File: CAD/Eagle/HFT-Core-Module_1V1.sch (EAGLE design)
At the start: 399 parts, among them Q0521 ABS07-32.768KHZ, Q0811 ABM03B-32.000MHZ, Q0911 ABM3B-16MHZ-10-R50-1-U, T1201 MMBT2222, T1202 MMBT2222, T1203 MMBT2222, U0111 STM32L4Z_144PIN_SMPS, U0431 PAM2305AAB120, U0601 LM4120IM5-3.0, U0611 MAX5217, U0631 CFPT-141-20MHZ, U0641 OPA354, U0701 Si5338, U0801 SX1276, U0901 AX5243, U0911 PE4259, U0921 PE4259, U0991 PE4259, U1101 MCP3911A0-E-SS, U1111 MAX5136AGTG+, U1131 OPA354, U1141 OPA354, U1201 NHD-C0220BIZ_2X20CHARS, U1301 MPU-9250, U1311 MS5607-02BA03, U1321 SHT31-DIS, U1402 SPV1040T, U1501 TS5A23166, U1601 SC189ZSKTRT, U1701 TS5A23166, U1801 TS5A23166, U1901 TS5A23166, X1261 TTE_EN11-HSM, X1401 WIRE-TO-BOARD_5MM08_1X02, X2001 MOLEX 105017-0001, X2101 SMA_SMT_AMPHENOL-901-143, SAM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, X2111 SMA_SMT_AMPHENOL-901-143, SAM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, X2201 CUI SJ1-3535NS, X2211 CUI SJ1-3535NS, X2311 2X20/90_1MM27_HARWIN_M50-3202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, X2312 2X20/90_1MM27_HARWIN_M50-3202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, X2321 2X20/90_1MM27_HARWIN_M50-3202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, X2322 2X20/90_1MM27_HARWIN_M50-3202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, X2331 2X20/90_1MM27_HARWIN_M50-3202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, X2332 2X20/90_1MM27_HARWIN_M50-3202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

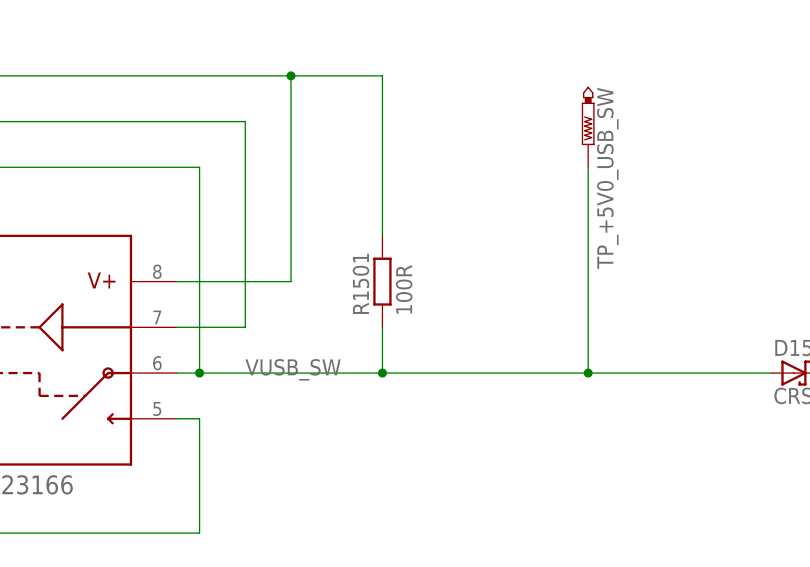
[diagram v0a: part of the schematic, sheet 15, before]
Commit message: HW_1V1 - USB-SW - Bybass resistor changed to 68R
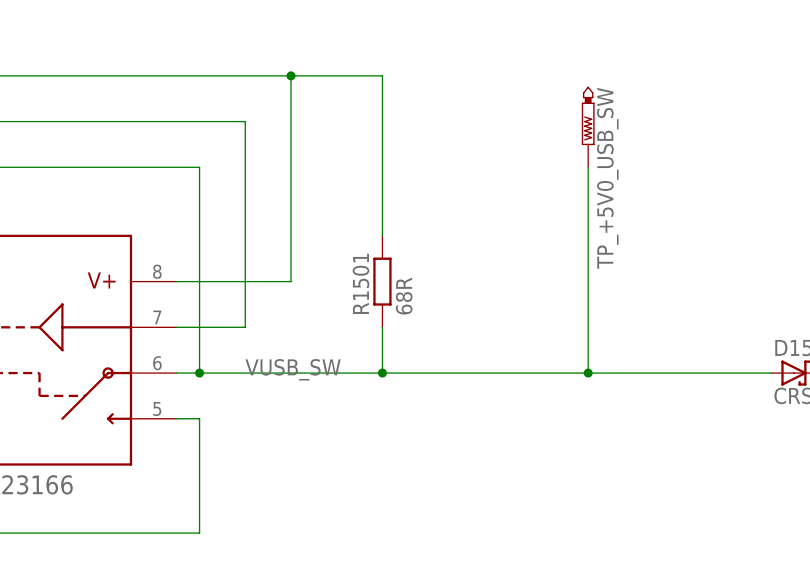
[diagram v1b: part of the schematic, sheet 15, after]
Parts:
- R1501: value 100R -> 68R
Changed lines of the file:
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@@
 <part name="R1412" library="rcl" deviceset="R-EU_" device="R0603" value="100kR"/>
 <part name="X1401" library="df4iah_connector" deviceset="WIRE-TO-BOARD_5MM08_1X02" device=""/>
-<part name="R1501" library="df4iah_rcl" deviceset="R-EU_" device="R0805" value="100R"/>
+<part name="R1501" library="df4iah_rcl" deviceset="R-EU_" device="R0805" value="68R"/>
 <part name="R0331" library="rcl" deviceset="R-EU_" device="R0603" value="100kR"/>
 <part name="R0332" library="rcl" deviceset="R-EU_" device="R0603" value="100kR"/>

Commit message: HW_1V1 - CAD/Eagle - Replacements for 9-axis controller and 1.8V supply
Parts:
- removed C0431, C0444: 10uF, rcl:C-EUC0805
- removed C0432: 100nF, rcl:C-EUC0603
- removed L0433: 2.2uH 14mR, df4iah_rcl:L-EU6.0X6.0MM
- removed TP_+1V2: PTR1B1,27, testpad:PTR1B1,27
- removed U0431: PAM2305AAB120, df4iah_powersupply:PAM2305
- added C0001, C0003: 10uF, rcl:C-EUC0805
- added C0002: 100nF, rcl:C-EUC0603
- added L0001: 2.2uH 14mR, df4iah_rcl:L-EU6.0X6.0MM
- added TP_+1V1: PTR1B1,27, testpad:PTR1B1,27
- added U0001: PAM2305AAB120, df4iah_powersupply:PAM2305
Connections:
- net +1V8_UNUSED renamed +1V8
- net +1V2: now also C0003.1, L0001.1, TP_+1V1.TP, U0001.VOUT_FB; no longer C0444.1, L0433.1, TP_+1V2.TP, U0431.VOUT_FB
- net +3V3: now also C0001.1, C0002.1, U0001.EN, U0001.VIN; no longer C0431.1, C0432.1, U0431.EN, U0431.VIN
- net GND: now also C0001.2, C0002.2, C0003.2, U0001.GND; no longer C0431.2, C0432.2, C0444.2, U0431.GND
- net VDD12_SW: now also L0001.2, U0001.SW; no longer L0433.2, U0431.SW
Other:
- note added: "12mA Start-up mode 2mA MPPT mode TODO: To be replaced by Texas Instruments BQ25570"
- note added: "MCU LF Osc"
- note added: "MCU Reset & SWD"
- note added: "MCU power distribution"
- note added: "MCU: low frequency oscillator"
- note added: "Power converter 3.3V --> 1.2V"
- note added: "Power converter 3.3V --> 1.8V"
- note added: "TODO: To be replaced by ICM-20948 (1.8 Volt !) Use SPI instead of I2C and Level Converter"
- note added: "VCTCXO 20MHz"
- note removed: "12mA Start-up mode 2mA MPPT mode"
- note removed: "Low frequency oscillator"

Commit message: HW_1V1 - CAD/Eagle - some more changes
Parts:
- removed C1301, C1303: 100nF, rcl:C-EUC0603
- removed C1302: 10nF, rcl:C-EUC0603
- removed D1403: CRS08, df4iah_diode:CRS08
- removed R1301: 68R, rcl:R-EU_R0603
- removed U1301: MPU-9250, df4iah_sensors:MPU-9250
- removed U1402: SPV1040T, df4iah_powersupply:SPV1040
- added C0004, C0005, C0007: 100nF, rcl:C-EUC0603
- added C0006: 10nF, rcl:C-EUC0603
- added R0001: 68R, rcl:R-EU_R0603
- added R0002, R0003: 68R, df4iah_rcl:R-EU_R0805
- added R0004, R0005: 2M, df4iah_rcl:R-EU_R0805
- added U0004: TS5A23166, df4iah_sc-switches:TS5A23166
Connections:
- net +1V8 renamed +1V8_UNUSED
- removed net MPU_REGOUT: C1303.1, U1301.REGOUT
- new net 3V3_9AXIS_VDD: U0004.6
- new net 3V3_9AXIS_VDDIO: R0005.1, U0004.2
- new net MCU_OUT_9AXIS_VDDIO_EN: R0002.1
- new net MCU_OUT_9AXIS_VDDIO_EN_R: R0002.2, R0004.2, U0004.7
- new net MCU_OUT_9AXIS_VDD_EN: R0003.1
- new net MCU_OUT_9AXIS_VDD_EN_R: R0003.2, R0005.2, U0004.3
- new net MPU_REGOUT1: C0005.1
- net +3V3: now also C0004.1, C0006.1, C0007.1, U0004.1, U0004.5, U0004.8; no longer C1301.1, C1302.1, U1301.!CS, U1301.VDD, U1301.VDDIO
- net GND: now also C0004.2, C0005.2, C0006.2, C0007.2, R0004.1, U0004.4; no longer C1301.2, C1302.2, C1303.2, U1301.AD0/SDO, U1301.FSYNC, U1301.GND, U1402.GND
- net MCU_I2C4_SCL: no longer U1301.SCL/SCLK
- net MCU_I2C4_SDA: no longer U1301.SDA/SDI
- net MPU_INT: now also R0001.1; no longer R1301.1, U1301.INT
- net PF13: now also R0001.2; no longer R1301.2
- net SPV_ICTRL_M: no longer U1402.ICTRL_M
- net SPV_ICTRL_P: no longer U1402.ICTRL_P
- net SPV_LX: no longer D1403.A, U1402.LX
- net SPV_VCTRL: no longer U1402.VCTRL
- net SPV_VOUT: no longer D1403.C, U1402.VOUT
- net VSOL: no longer U1402.MPP_SET, U1402.XSHUT
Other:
- note added: "9-axis sensor"
- note added: "Audio ADC/DAC"
- note added: "BQ25570: 2V->5V: 91% 0μA5 5V->3V3: 89% 0μA05"
- note added: "Electronic switch for 3V3 --> 9-axis-sensor Vdd_io and Vdd"
- note added: "LCD / Rotary Enc."
- note added: "PLL"
- note added: "PLL - clock distributor I2C addr: 0x70"
- note added: "PMIC - Solar power"
- note added: "Radio AX5243"
- note added: "Radio SX1262 1/2"
- note added: "Radio SX1262 2/2"
- note added: "Rel. humidity sensor: Sensirion SHT3x I2C addr: 0x44"
- note added: "SPI: 9-axis MEMS-MotionTracking sensor"
- note added: "SPI: Audio stereo A/D-Converter"
- note added: "SPI: Audio stereo D/A-Converter"
- note added: "SPI: Radio AX5243 - channel 1"
- note added: "SPI: Radio SX1262 - channel 2"
- note added: "SW 3V3 --> 9-axis"
- note added: "TODO: To be replaced by LSM9DS1 Use SPI instead of I2C. Power on sequencing needed !"
- note added: "TODO: remove me! (--> PMIC solar)"
- note added: "TPS62051DGSR: 87% 12μA"
- note added: "Vdd shall be risen 0ms .. 10ms later than Vdd_io !"
- note added: "Weather sensors"
- note removed: "9-axis sensor: MPU-9250 I2C addr: 0x68 / 0x0C"
- note removed: "Audio stereo A/D-Converter SPI"
- note removed: "Audio stereo D/A-Converter SPI"
- note removed: "Clock distributor I2C addr: 0x70"
- note removed: "Power converter 3.3V --> 1.8V"
- note removed: "RH sensor: Sensirion SHT3x I2C addr: 0x44"
- note removed: "TODO: ENABLE to MCU GPIO out +3V3 to MCU ADC to be replaced by TPS62056DGSR"
- note removed: "TODO: To be replaced by ICM-20948 (1.8 Volt !) Use SPI instead of I2C and Level Converter"
- note removed: "VHF / UHF AX5243 - channel 2 SPI"
- note removed: "VHF / UHF SX1276 - channel 1 SPI"

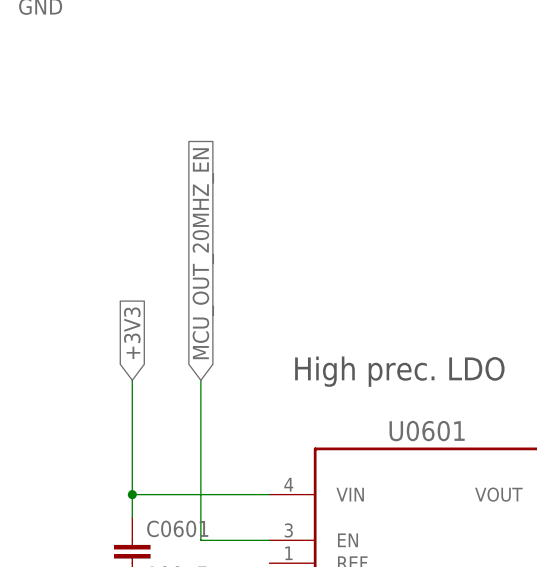
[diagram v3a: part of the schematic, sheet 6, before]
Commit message: HW_1V1 - CAD/Eagle - U0601 VIN changed to +3V3 rail
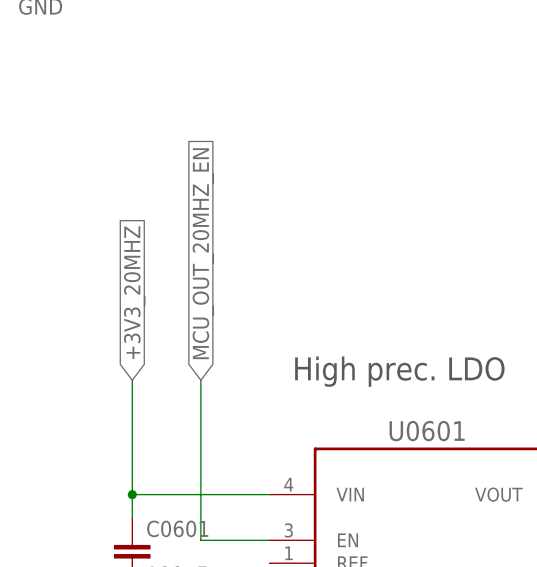
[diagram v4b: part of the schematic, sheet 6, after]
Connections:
- net +3V3: no longer C0601.1, U0601.VIN
- net +3V3_20MHZ: now also C0601.1, U0601.VIN
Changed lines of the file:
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@@
-</segment>
-</net>
-<net name="+3V3" class="0">
-<segment>
-<pinref part="U0601" gate="A" pin="VIN"/>
-<wire x1="20.32" y1="58.42" x2="35.56" y2="58.42" width="0.1524" layer="91"/>
-<junction x="20.32" y="58.42"/>
-<pinref part="C0601" gate="G$1" pin="1"/>
-<wire x1="20.32" y1="58.42" x2="20.32" y2="55.88" width="0.1524" layer="91"/>
-<wire x1="20.32" y1="71.12" x2="20.32" y2="58.42" width="0.1524" layer="91"/>
-<label x="20.32" y="71.12" size="1.778" layer="95" rot="R90" xref="yes"/>
 </segment>
 </net>
@@
 <junction x="17.78" y="142.24"/>
 </segment>
+<segment>
+<pinref part="U0601" gate="A" pin="VIN"/>
+<wire x1="20.32" y1="58.42" x2="35.56" y2="58.42" width="0.1524" layer="91"/>
+<junction x="20.32" y="58.42"/>
+<pinref part="C0601" gate="G$1" pin="1"/>
+<wire x1="20.32" y1="58.42" x2="20.32" y2="55.88" width="0.1524" layer="91"/>
+<wire x1="20.32" y1="71.12" x2="20.32" y2="58.42" width="0.1524" layer="91"/>
+<label x="20.32" y="71.12" size="1.778" layer="95" rot="R90" xref="yes"/>
+</segment>
 </net>

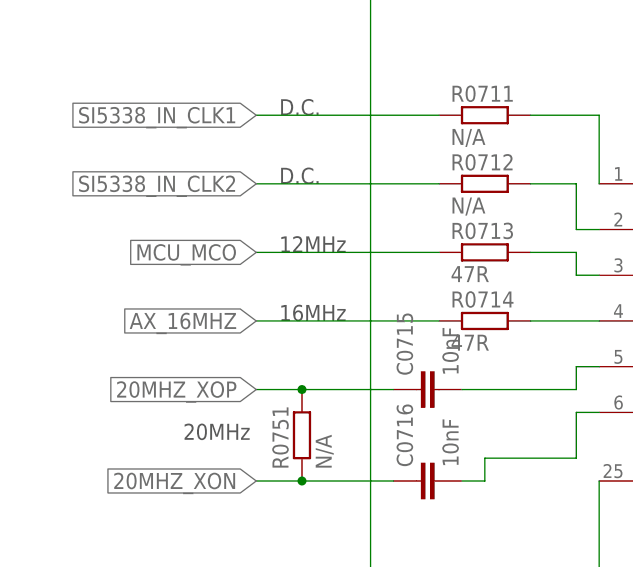
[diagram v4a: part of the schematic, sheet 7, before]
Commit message: HW_1V1 - CAD/Eagle - AX5243 clock out is 8MHz
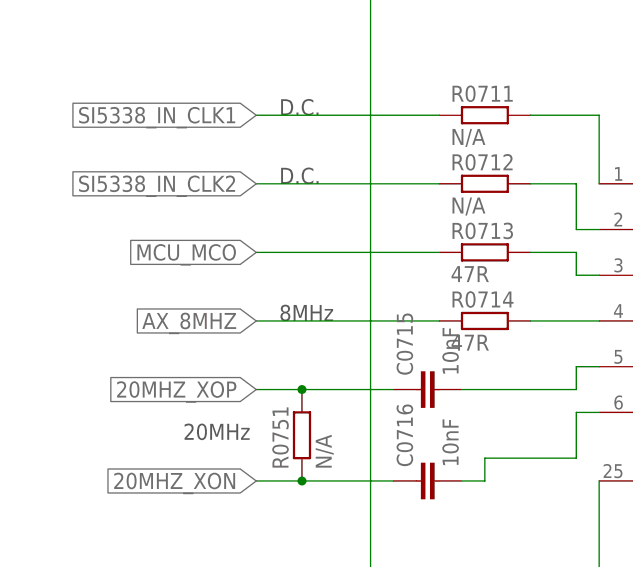
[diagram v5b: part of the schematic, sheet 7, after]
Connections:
- net AX_16MHZ renamed AX_8MHZ
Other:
- note added: "8MHz"
- note removed: "12MHz"
- note removed: "16MHz"
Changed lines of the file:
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@@
 I2C addr: 0x70</text>
 <text x="118.364" y="38.1" size="1.778" layer="97" rot="R90">10MHz</text>
-<text x="50.8" y="88.9" size="1.778" layer="97">16MHz</text>
+<text x="50.8" y="88.9" size="1.778" layer="97">8MHz</text>
 <text x="40.132" y="75.692" size="1.778" layer="97">20MHz</text>
 <text x="50.8" y="111.76" size="1.778" layer="97">D.C.</text>
 <text x="50.8" y="104.14" size="1.778" layer="97">D.C.</text>
-<text x="50.8" y="96.52" size="1.778" layer="97">12MHz</text>
 <text x="101.6" y="23.622" size="1.778" layer="97" rot="R90">MCU_EXTI7_INTR_SI5338</text>
 <text x="122.936" y="22.098" size="1.778" layer="97" rot="R90">MCU_HSE</text>
@@
 </segment>
 </net>
-<net name="AX_16MHZ" class="0">
+<net name="AX_8MHZ" class="0">
 <segment>
 <wire x1="48.26" y1="88.9" x2="68.58" y2="88.9" width="0.1524" layer="91"/>
@@
 </segment>
 </net>
-<net name="AX_16MHZ" class="0">
+<net name="AX_8MHZ" class="0">
 <segment>
 <wire x1="147.32" y1="114.3" x2="220.98" y2="114.3" width="0.1524" layer="91"/>

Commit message: HW_1V1 - CAD/Eagle - remove many signals from MCU switchboard
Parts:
- removed C0004, C0005, C0007: 100nF, rcl:C-EUC0603
- removed C0006: 10nF, rcl:C-EUC0603
- removed R0005: 2M, df4iah_rcl:R-EU_R0805
- removed R0201, R0202, R0211, R0212, R0221, R0222, R0231, R0232: 0R, rcl:R-EU_R0603
- removed R0241, R0242, R0243, R0251, R0252, R0253, R0254, R0269, R0271, R0272, R0273, R0274, R0275, R0276, R0277, R0281, R0282, R0283, R0284, R0285, R0286, R0287, R0288, R0289, R0290, R0291, R0292, R0293, R0294, R0295, R0296: 47R, rcl:R-EU_R0603
- removed U0004: TS5A23166, df4iah_sc-switches:TS5A23166
- added C1301, C1303: 100nF, rcl:C-EUC0603
- added C1302: 10nF, rcl:C-EUC0603
- added D1403: CRS08, df4iah_diode:CRS08
- added R0691, R0692, R2391, R2392, R2393, R2394, R2395, R2396: 0R, rcl:R-EU_R0603
- added R0891, R0892, R0893, R0951, R1091, R1281, R1511, R1711, R1811, R1901, R2361, R2362, R2363, R2364, R2365, R2366, R2367, R2368, R2369, R2370, R2371, R2372, R2373, R2374, R2375, R2381, R2382, R2383, R2384, R2385, R2386, R2387, R2388, R2389: 47R, rcl:R-EU_R0603
- added R1301: 68R, rcl:R-EU_R0603
- added U1301: MPU-9250, df4iah_sensors:MPU-9250
- added U1402: SPV1040T, df4iah_powersupply:SPV1040
- R0001: value 68R -> 47R
- R0002, R0003: value 68R -> 47R; device df4iah_rcl:R-EU_R0805 -> rcl:R-EU_R0603
- R0004: value 2M -> 47R; device df4iah_rcl:R-EU_R0805 -> rcl:R-EU_R0603
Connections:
- removed net 3V3_9AXIS_VDD: U0004.6
- removed net 3V3_9AXIS_VDDIO: R0005.1, U0004.2
- removed net MCU_I2C1_SCL: R0201.2, X2312.7
- removed net MCU_I2C1_SDA: R0202.2, X2312.8
- removed net MCU_I2C2_SCL: R0211.2, X2322.7
- removed net MCU_I2C2_SDA: R0212.2, X2322.8
- removed net MCU_I2C3_SCL: R0221.2, X2332.7
- removed net MCU_I2C3_SDA: R0222.2, X2332.8
- removed net MCU_MCO: R0271.2, R0713.1
- removed net MCU_OUT_9AXIS_VDDIO_EN: R0002.1
- removed net MCU_OUT_9AXIS_VDDIO_EN_R: R0002.2, R0004.2, U0004.7
- removed net MCU_OUT_9AXIS_VDD_EN: R0003.1
- removed net MCU_OUT_9AXIS_VDD_EN_R: R0003.2, R0005.2, U0004.3
- removed net MCU_SPI1_MISO: R0243.2, X2312.12, X2322.12, X2332.12
- removed net MCU_SPI1_MOSI: R0242.2, X2312.11, X2322.11, X2332.11
- removed net MCU_SPI1_SCK: R0241.2, X2312.13, X2322.13, X2332.13
- removed net MCU_WAKEUP: R0269.2, X2311.33, X2321.33, X2331.33
- removed net MPU_REGOUT1: C0005.1
- new net I2C1_N_SCL: R2391.2, X2312.7
- new net I2C1_N_SDA: R2392.2, X2312.8
- new net I2C2_W_SCL: R2393.2, X2322.7
- new net I2C2_W_SDA: R2394.2, X2322.8
- new net I2C3_S_SCL: R2395.2, X2332.7
- new net I2C3_S_SDA: R2396.2, X2332.8
- new net MCU_WAKEUP_N: R2371.2, X2311.33
- new net MCU_WAKEUP_S: R2373.2, X2331.33
- new net MCU_WAKEUP_W: R2372.2, X2321.33
- new net MPU_REGOUT: C1303.1, U1301.REGOUT
- new net SPI1_N_MISO: R2382.2, X2312.12
- new net SPI1_N_MOSI: R2381.2, X2312.11
- new net SPI1_N_SCK: R2383.2, X2312.13
- new net SPI1_S_MISO: R2388.2, X2332.12
- new net SPI1_S_MOSI: R2387.2, X2332.11
- new net SPI1_S_SCK: R2389.2, X2332.13
- new net SPI1_W_MISO: R2385.2, X2322.12
- new net SPI1_W_MOSI: R2384.2, X2322.11
- new net SPI1_W_SCK: R2386.2, X2322.13
- net +3V3: now also C1301.1, C1302.1, U1301.!CS, U1301.VDD, U1301.VDDIO; no longer C0004.1, C0006.1, C0007.1, U0004.1, U0004.5, U0004.8
- net +3V3_20MHZ: now also U0601.EN
- net GND: now also C1301.2, C1302.2, C1303.2, U1301.AD0/SDO, U1301.FSYNC, U1301.GND, U1402.GND; no longer C0004.2, C0005.2, C0006.2, C0007.2, R0004.1, U0004.4
- net I2S_FS_OUT: now also R0004.2; no longer R0284.2
- net I2S_MCLK_OUT: now also R0003.2; no longer R0283.2
- net I2S_SCK_OUT: now also R0001.2; no longer R0281.2
- net I2S_SD_OUT: now also R0002.2; no longer R0282.2
- net MCU_I2C4_SCL: now also R0691.2, U1301.SCL/SCLK; no longer R0231.2
- net MCU_I2C4_SDA: now also R0692.2, U1301.SDA/SDI; no longer R0232.2
- net MCU_OUT_20MHZ_EN: now also R1811.2; no longer R0273.2, U0601.EN
- net MCU_OUT_AX_SEL: now also R1091.2; no longer R0253.2
- net MCU_OUT_HICUR_EN: now also R1711.2; no longer R0275.2
- net MCU_OUT_LCD_NRST: now also R1281.1; no longer R0272.2
- net MCU_OUT_SX_HF_!LF!_CTRL: now also R0951.2; no longer R0277.2
- net MCU_OUT_SX_SEL: now also R0893.2; no longer R0254.2
- net MCU_OUT_VDD12_EN: now also R1901.2; no longer R0276.2
- net MCU_OUT_VUSB_EN: now also R1511.2; no longer R0274.2
- net MCU_SPI3_MOSI: now also R0892.2; no longer R0252.2
- net MCU_SPI3_SCK: now also R0891.2; no longer R0251.2, U0801.SCLK
- net MPU_INT: now also R1301.1, U1301.INT; no longer R0001.1
- net PA0: now also R2368.1; no longer R0292.1
- net PA2: now also R2365.1; no longer R0289.1
- net PA6: now also R2375.1; no longer R0296.1
- net PA8: now also R0713.1; no longer R0271.1
- net PB1: now also R2374.1; no longer R0295.1
- net PC0: now also R1901.1; no longer R0276.1
- net PC1: now also R1711.1; no longer R0275.1
- net PC10: now also R0891.1; no longer R0251.1
- net PC12: now also R0892.1; no longer R0252.1
- net PC13: now also R2371.1, R2372.1, R2373.1; no longer R0269.1
- net PC2: now also R1511.1; no longer R0274.1
- net PC3: now also R1811.1; no longer R0273.1
- net PC4: now also R2369.1; no longer R0293.1
- net PC5: now also R2370.1; no longer R0294.1
- net PD13: now also R0692.1; no longer R0232.1
- net PD4: now also R2367.1; no longer R0291.1
- net PD6: now also R2366.1; no longer R0290.1
- net PE10: now also R0003.1; no longer R0283.1
- net PE11: now also R1091.1; no longer R0253.1
- net PE12: now also R0893.1; no longer R0254.1
- net PE13: now also R2383.1, R2386.1, R2389.1; no longer R0241.1
- net PE14: now also R2382.1, R2385.1, R2388.1; no longer R0243.1
- net PE15: now also R2381.1, R2384.1, R2387.1; no longer R0242.1
- net PE3: now also R0002.1; no longer R0282.1
- net PE8: now also R0001.1; no longer R0281.1
- net PE9: now also R0004.1; no longer R0284.1
- net PF0: now also R2394.1; no longer R0212.1
- net PF1: now also R2393.1; no longer R0211.1
- net PF12: now also R1281.2; no longer R0272.1
- net PF13: now also R1301.2; no longer R0001.2
- net PF14: now also R0691.1; no longer R0231.1
- net PG0: now also R0951.1; no longer R0277.1
- net PG10: now also R2362.1; no longer R0286.1
- net PG11: now also R2364.1; no longer R0288.1
- net PG12: now also R2363.1; no longer R0287.1
- net PG13: now also R2392.1; no longer R0202.1
- net PG14: now also R2391.1; no longer R0201.1
- net PG7: now also R2395.1; no longer R0221.1
- net PG8: now also R2396.1; no longer R0222.1
- net PG9: now also R2361.1; no longer R0285.1
- net SPV_ICTRL_M: now also U1402.ICTRL_M
- net SPV_ICTRL_P: now also U1402.ICTRL_P
- net SPV_LX: now also D1403.A, U1402.LX
- net SPV_VCTRL: now also U1402.VCTRL
- net SPV_VOUT: now also D1403.C, U1402.VOUT
- net UART1_CTS_IN: now also R2364.2; no longer R0288.2
- net UART1_RTS_OUT: now also R2363.2; no longer R0287.2
- net UART1_RX_IN: now also R2362.2; no longer R0286.2
- net UART1_TX_OUT: now also R2361.2; no longer R0285.2
- net UART2_CTS_IN: now also R2368.2; no longer R0292.2
- net UART2_RTS_OUT: now also R2367.2; no longer R0291.2
- net UART2_RX_IN: now also R2366.2; no longer R0290.2
- net UART2_TX_OUT: now also R2365.2; no longer R0289.2
- net UART3_CTS_IN: now also R2375.2; no longer R0296.2
- net UART3_RTS_OUT: now also R2374.2; no longer R0295.2
- net UART3_RX_IN: now also R2370.2; no longer R0294.2
- net UART3_TX_OUT: now also R2369.2; no longer R0293.2
- net VSOL: now also U1402.MPP_SET, U1402.XSHUT
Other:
- note added: "9-axis sensor: MPU-9250 I2C addr: 0x68 / 0x0C"
- note added: "Audio stereo A/D-Converter SPI"
- note added: "Audio stereo D/A-Converter SPI"
- note added: "Clock distributor I2C addr: 0x70"
- note added: "MCU_MCO"
- note added: "RH sensor: Sensirion SHT3x I2C addr: 0x44"
- note added: "TODO: ENABLE to MCU GPIO out +3V3 to MCU ADC to be replaced by TPS62056DGSR"
- note added: "TODO: To be replaced by ICM-20948 (1.8 Volt !) Use SPI instead of I2C and Level Converter"
- note added: "VHF / UHF AX5243 - channel 2 SPI"
- note added: "VHF / UHF SX1276 - channel 1 SPI"
- note removed: "9-axis sensor"
- note removed: "Audio ADC/DAC"
- note removed: "BQ25570: 2V->5V: 91% 0μA5 5V->3V3: 89% 0μA05"
- note removed: "D.C."
- note removed: "Electronic switch for 3V3 --> 9-axis-sensor Vdd_io and Vdd"
- note removed: "LCD / Rotary Enc."
- note removed: "PLL"
- note removed: "PLL - clock distributor I2C addr: 0x70"
- note removed: "PMIC - Solar power"
- note removed: "Radio AX5243"
- note removed: "Radio SX1262 1/2"
- note removed: "Radio SX1262 2/2"
- note removed: "Rel. humidity sensor: Sensirion SHT3x I2C addr: 0x44"
- note removed: "SPI: 9-axis MEMS-MotionTracking sensor"
- note removed: "SPI: Audio stereo A/D-Converter"
- note removed: "SPI: Audio stereo D/A-Converter"
- note removed: "SPI: Radio AX5243 - channel 1"
- note removed: "SPI: Radio SX1262 - channel 2"
- note removed: "SW 3V3 --> 9-axis"
- note removed: "TODO: To be replaced by LSM9DS1 Use SPI instead of I2C. Power on sequencing needed !"
- note removed: "TODO: remove me! (--> PMIC solar)"
- note removed: "TPS62051DGSR: 87% 12μA"
- note removed: "Vdd shall be risen 0ms .. 10ms later than Vdd_io !"
- note removed: "Weather sensors"

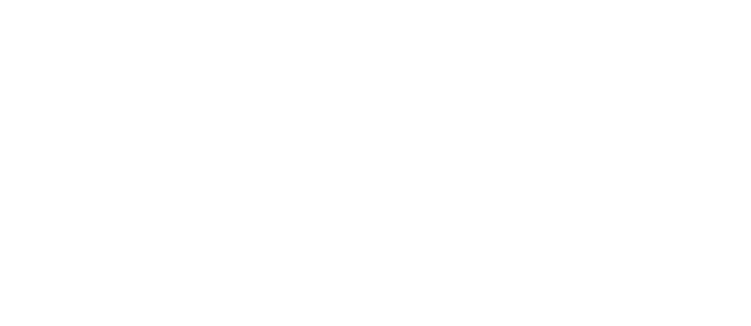
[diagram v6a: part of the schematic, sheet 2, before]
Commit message: HW_1V1 - CAD/Eagle - Note added for QUADSPI to include to new design
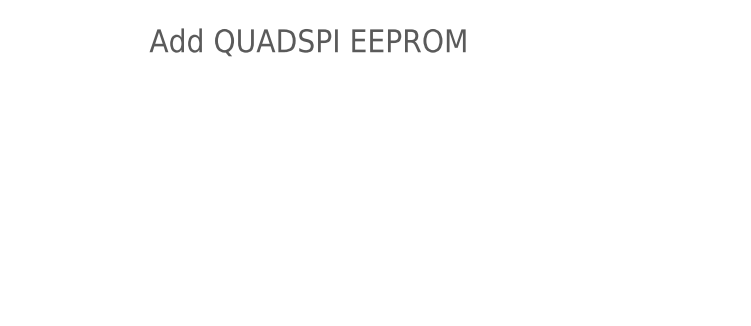
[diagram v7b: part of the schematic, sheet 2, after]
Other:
- note added: "Add QUADSPI EEPROM"
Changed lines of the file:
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@@
 <text x="231.14" y="106.68" size="1.778" layer="97">MCU_PWM_LED_G</text>
 <text x="231.14" y="101.6" size="1.778" layer="97">MCU_PWM_LED_B</text>
+<text x="33.02" y="142.24" size="2.54" layer="97">Add QUADSPI EEPROM</text>
 </plain>
 <instances>
